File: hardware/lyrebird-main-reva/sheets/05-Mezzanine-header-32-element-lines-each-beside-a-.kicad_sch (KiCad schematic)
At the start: 9 parts, among them J2 Mezzanine 2x40

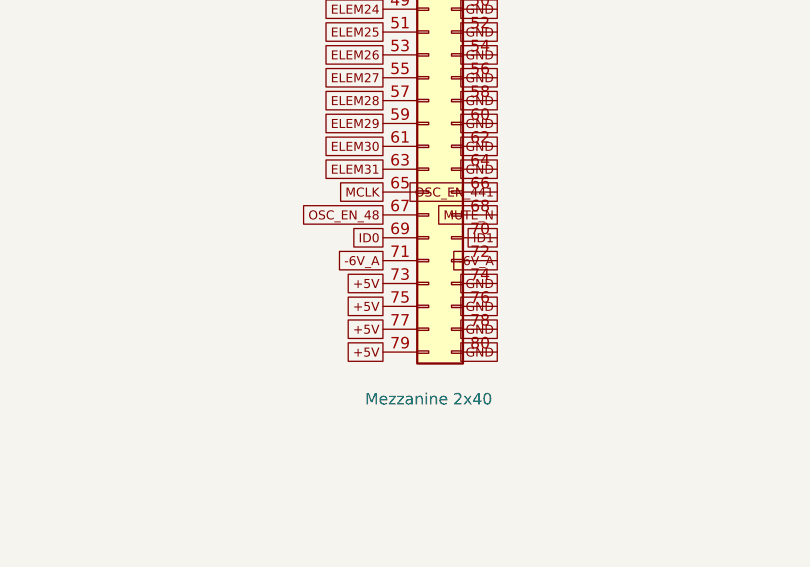
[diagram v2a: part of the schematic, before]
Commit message: Flank the negative rail with ground, and keep the power review
The power validator found the pin map I wrote put -6V_A in the column
immediately beside ID1. On a 2x40 odd/even header pins 2k-1 and 2k share
a column, and the control block -- MCLK, both oscillator enables, MUTE_N
and both ID straps, pins 65 to 70 -- has no ground pin inside it at all.
One bridge or one whisker across 1.27 mm would have put -6 V on a net
that reaches a GateMate GPIO through nothing but a 10 k pull-down, with
the input's clamp diode conducting and the current limited only by the
bridge.

The pair is now column 37, with full ground columns at 71/72 and 75/76
either side. Adjacent to itself still, so a half-inserted connector
cannot present one without the other -- that part of the original
reasoning was right and is kept. Four pins out of a ground surplus.

Both halves of the connector were regenerated and still agree on all 80
pins, which is the check this change lives or dies by: two files
independently walk the same pin list in the same order, and nothing but
that agreement makes the boards mate.

interface.md carries the rule rather than just the pin numbers, because
the reason is the part a future module designer needs.

Co-Authored-By: Claude Opus 5 <noreply@anthropic.com>
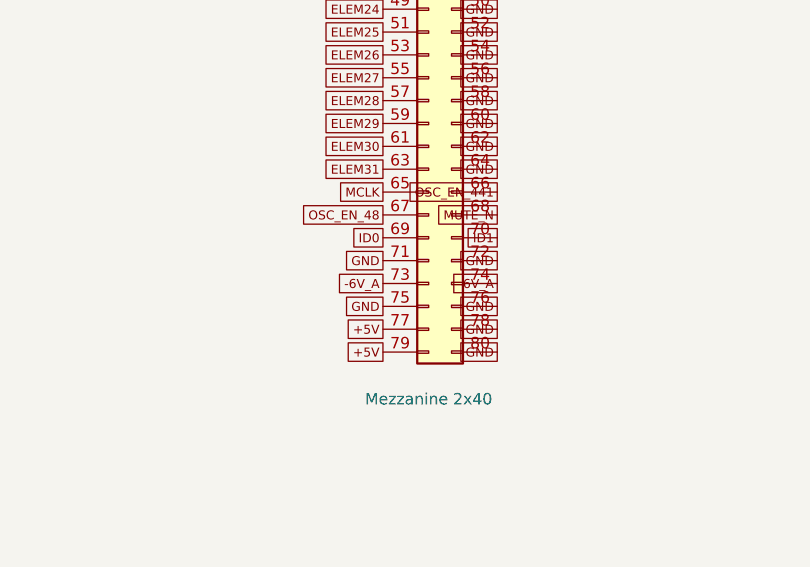
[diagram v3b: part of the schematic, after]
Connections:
- net +5V: no longer J2.73 (Pin_73), J2.75 (Pin_75)
- net -6V_A: now also J2.73 (Pin_73), J2.74 (Pin_74); no longer J2.71 (Pin_71), J2.72 (Pin_72)
- net GND: now also J2.71 (Pin_71), J2.72 (Pin_72), J2.75 (Pin_75); no longer J2.74 (Pin_74)
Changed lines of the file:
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@@
-		(effects (font (size 1.0 1.0)) (justify right))
-)
-	(global_label "+5V" (shape passive) (at 81.28 172.72 0)
-		(effects (font (size 1.0 1.0)) (justify right))
-)
-	(global_label "+5V" (shape passive) (at 81.28 175.26 0)
 		(effects (font (size 1.0 1.0)) (justify right))
 )
@@
 		(effects (font (size 1.0 1.0)) (justify right))
 )
-	(global_label "-6V_A" (shape passive) (at 81.28 170.18 0)
-		(effects (font (size 1.0 1.0)) (justify right))
-)
-	(global_label "-6V_A" (shape passive) (at 93.98 170.18 0)
+	(global_label "-6V_A" (shape passive) (at 81.28 172.72 0)
+		(effects (font (size 1.0 1.0)) (justify right))
+)
+	(global_label "-6V_A" (shape passive) (at 93.98 172.72 0)
 		(effects (font (size 1.0 1.0)) (justify right))
 )
@@
 		(effects (font (size 1.0 1.0)) (justify right))
 )
-	(global_label "GND" (shape passive) (at 93.98 172.72 0)
-		(effects (font (size 1.0 1.0)) (justify right))
-)
+	(global_label "GND" (shape passive) (at 81.28 170.18 0)
+		(effects (font (size 1.0 1.0)) (justify right))
+)
+	(global_label "GND" (shape passive) (at 93.98 170.18 0)
+		(effects (font (size 1.0 1.0)) (justify right))
+)
+	(global_label "GND" (shape passive) (at 81.28 175.26 0)
+		(effects (font (size 1.0 1.0)) (justify right))
+)
